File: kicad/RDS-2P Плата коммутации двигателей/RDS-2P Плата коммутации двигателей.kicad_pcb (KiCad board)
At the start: 2 copper layers, 100 x 100 mm, 12 parts, among them J1 XT30U, J2 XT30U, J3 5264-3AW, J4 5264-3AW, J5 5264-3AW, J6 5264-3AW, J7 Conn_01x01_Pin, J8 Conn_01x01_Pin, J9 Conn_01x01_Pin, U1 Converter_Mini560

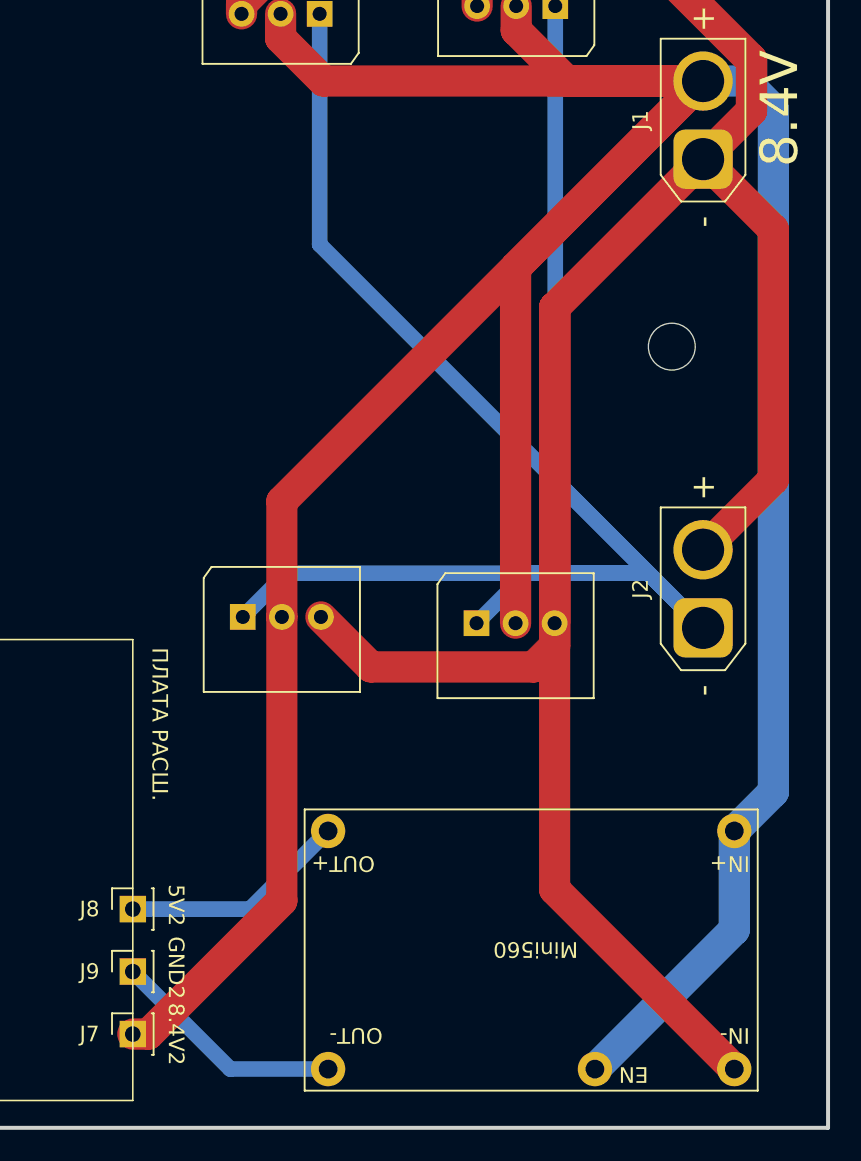
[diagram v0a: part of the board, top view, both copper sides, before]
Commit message: Fix: pinout Mini560
Исправил распиновку Mini560 на платах
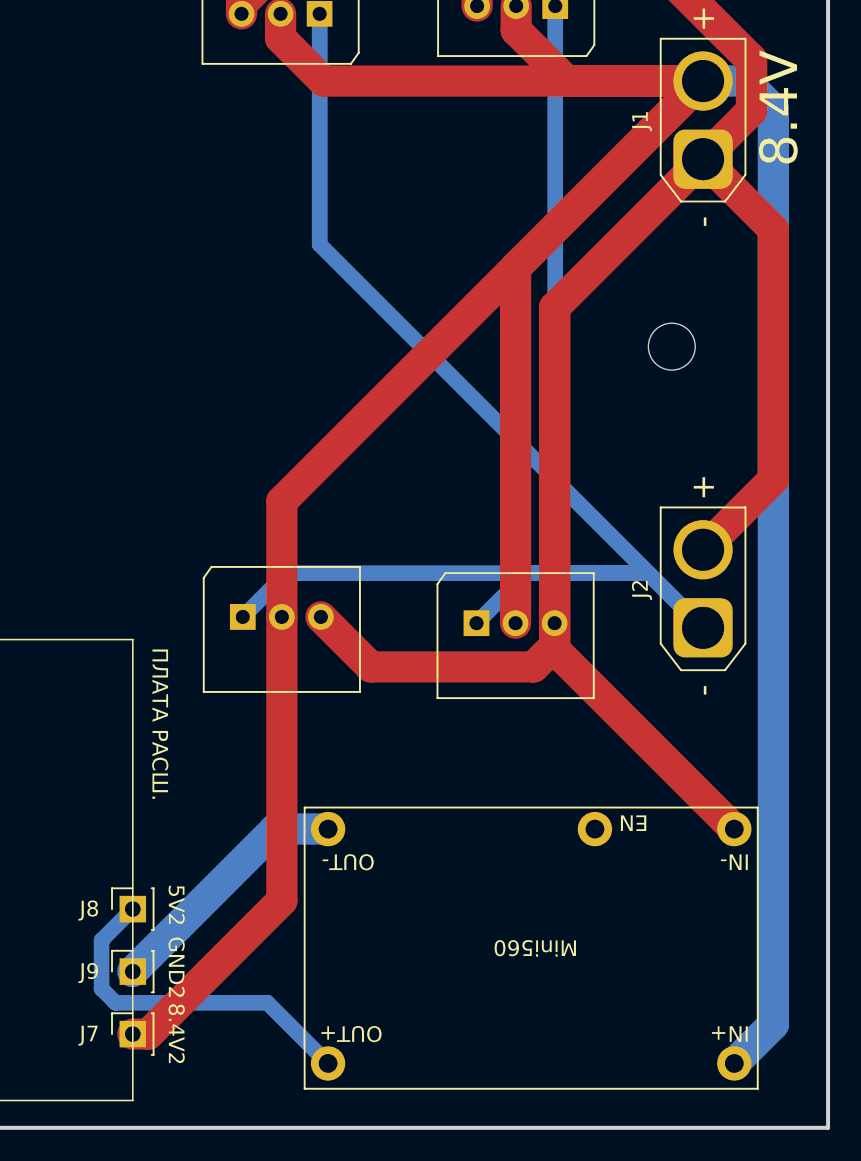
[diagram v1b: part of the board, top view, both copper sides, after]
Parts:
- moved U1 0.12 mm to (180.0, 131.9)
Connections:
- U1 pad 5: +8.4V -> 0 1
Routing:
- net 0: track 224.9 -> 189.3 mm
- net Net-(J8-Pin_1): track 14.6 -> 22.4 mm
- net +8.4V: track 232.4 -> 228.3 mm
- net Net-(J9-Pin_1): track 15.1 -> 16.3 mm
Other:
- board text removed: "EN"
- board text removed: "IN+"
- board text removed: "IN-"
- board text removed: "Mini560"
- board text removed: "OUT+"
- board text removed: "OUT-"
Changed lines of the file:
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@@
 	(net 4 "Net-(J8-Pin_1)")
 	(net 5 "Net-(J9-Pin_1)")
+	(net 6 "0 1")
 	(footprint "Connector_PinSocket_2.54mm:PinSocket_1x01_P2.54mm_Vertical"
 		(layer "F.Cu")
@@
 		(property ki_fp_filters "Connector*:*_1x??_*")
 		(sheetname "/")
-		(sheetfile "Плата коммутации двигателей для RDS-2P.kicad_sch")
+		(sheetfile "RDS-2P Плата коммутации двигателей.kicad_sch")
 		(attr through_hole)
 		(fp_line
@@
 		)
 		(sheetname "/")
-		(sheetfile "Плата коммутации двигателей для RDS-2P.kicad_sch")
+		(sheetfile "RDS-2P Плата коммутации двигателей.kicad_sch")
 		(fp_line
 			(start -2.5 4.8)
@@
 		(property ki_fp_filters "Connector*:*_1x??_*")
 		(sheetname "/")
-		(sheetfile "Плата коммутации двигателей для RDS-2P.kicad_sch")
+		(sheetfile "RDS-2P Плата коммутации двигателей.kicad_sch")
 		(attr through_hole)
 		(fp_line
@@
 		)
 		(sheetname "/")
-		(sheetfile "Плата коммутации двигателей для RDS-2P.kicad_sch")
+		(sheetfile "RDS-2P Плата коммутации двигателей.kicad_sch")
 		(fp_line
 			(start 7.5 4.8)
@@
 		)
 		(sheetname "/")
-		(sheetfile "Плата коммутации двигателей для RDS-2P.kicad_sch")
+		(sheetfile "RDS-2P Плата коммутации двигателей.kicad_sch")
 		(attr through_hole)
 		(fp_line
@@
 		)
 		(sheetname "/")
-		(sheetfile "Плата коммутации двигателей для RDS-2P.kicad_sch")
+		(sheetfile "RDS-2P Плата коммутации двигателей.kicad_sch")
 		(fp_line
 			(start -2.5 4.8)
@@
 		(property ki_fp_filters "Connector*:*_1x??_*")
 		(sheetname "/")
-		(sheetfile "Плата коммутации двигателей для RDS-2P.kicad_sch")
+		(sheetfile "RDS-2P Плата коммутации двигателей.kicad_sch")
 		(attr through_hole)
 		(fp_line
@@
 	(footprint "Library:Regulator_Mini560_5V"
 		(layer "F.Cu")
-		(at 180 132 180)
+		(at 180 131.88 180)
 		(property "Reference" "U1"
 			(at 13 -18.5 0)
@@
 		)
 		(sheetname "/")
-		(sheetfile "Плата коммутации двигателей для RDS-2P.kicad_sch")
+		(sheetfile "RDS-2P Плата коммутации двигателей.kicad_sch")
 		(fp_line
 			(start 27.5 1.38)
@@
 			(layer "F.CrtYd")
 		)
+		(fp_text user "Mini560"
+			(at 10 -7 180)
+			(unlocked yes)
+			(layer "F.SilkS")
+			(effects
+				(font
+					(size 1 1)
+					(thickness 0.1)
+				)
+				(justify left bottom)
+			)
+		)
+		(fp_text user "EN"
+			(at 5.5 1 180)
+			(unlocked yes)
+			(layer "F.SilkS")
+			(effects
+				(font
+					(size 1 1)
+					(thickness 0.1)
+				)
+				(justify left bottom)
+			)
+		)
+		(fp_text user "IN-"
+			(at -1 -1.5 180)
+			(unlocked yes)
+			(layer "F.SilkS")
+			(effects
+				(font
+					(size 1 1)
+					(thickness 0.1)
+				)
+				(justify left bottom)
+			)
+		)
+		(fp_text user "OUT-"
+			(at 23 -1.5 180)
+			(unlocked yes)
+			(layer "F.SilkS")
+			(effects
+				(font
+					(size 1 1)
+					(thickness 0.1)
+				)
+				(justify left bottom)
+			)
+		)
+		(fp_text user "OUT+"
+			(at 22.5 -12.5 180)
+			(unlocked yes)
+			(layer "F.SilkS")
+			(effects
+				(font
+					(size 1 1)
+					(thickness 0.1)
+				)
+				(justify left bottom)
+			)
+		)
+		(fp_text user "IN+"
+			(at -1 -12.5 180)
+			(unlocked yes)
+			(layer "F.SilkS")
+			(effects
+				(font
+					(size 1 1)
+					(thickness 0.1)
+				)
+				(justify left bottom)
+			)
+		)
 		(pad "1" thru_hole circle
-			(at 0 0 180)
+			(at 0 -15 180)
 			(size 2.2 2.2)
 			(drill 1.2)
@@
 		)
 		(pad "2" thru_hole circle
-			(at 0 -15.24 180)
+			(at 0 0 180)
 			(size 2.2 2.2)
 			(drill 1.2)
@@
 		)
 		(pad "3" thru_hole circle
-			(at 26 0 180)
+			(at 26 -15 180)
 			(size 2.2 2.2)
 			(drill 1.2)
@@
 		)
 		(pad "4" thru_hole circle
-			(at 26 -15.24 180)
+			(at 26 0 180)
 			(size 2.2 2.2)
 			(drill 1.2)
@@
 		)
 		(pad "5" thru_hole circle
-			(at 8.92 -15.24 180)
+			(at 8.92 0 180)
 			(size 2.2 2.2)
 			(drill 1.2)
 			(layers "*.Cu" "*.Mask")
 			(remove_unused_layers no)
-			(net 1 "+8.4V")
+			(net 6 "0 1")
 			(pinfunction "EN")
 			(pintype "input")
@@
 		)
 		(sheetname "/")
-		(sheetfile "Плата коммутации двигателей для RDS-2P.kicad_sch")
+		(sheetfile "RDS-2P Плата коммутации двигателей.kicad_sch")
 		(attr through_hole)
 		(fp_line
@@
 		)
 		(sheetname "/")
-		(sheetfile "Плата коммутации двигателей для RDS-2P.kicad_sch")
+		(sheetfile "RDS-2P Плата коммутации двигателей.kicad_sch")
 		(fp_line
 			(start 7.5 4.8)
@@
 		)
 	)
-	(gr_text "OUT-"
-		(at 157.5 144.5 180)
-		(layer "F.SilkS")
-		(effects
-			(font
-				(size 1 1)
-				(thickness 0.1)
-			)
-			(justify left bottom)
-		)
-	)
-	(gr_text "OUT+"
-		(at 157 133.5 180)
-		(layer "F.SilkS")
-		(effects
-			(font
-				(size 1 1)
-				(thickness 0.1)
-			)
-			(justify left bottom)
-		)
-	)
-	(gr_text "EN"
-		(at 174.5 147 180)
-		(layer "F.SilkS")
-		(effects
-			(font
-				(size 1 1)
-				(thickness 0.1)
-			)
-			(justify left bottom)
-		)
-	)
 	(gr_text "ПЛАТА РАСШ."
 		(at 142.635477 120.25 270)
@@
 		)
 	)
-	(gr_text "IN-"
-		(at 181 144.5 180)
-		(layer "F.SilkS")
-		(effects
-			(font
-				(size 1 1)
-				(thickness 0.1)
-			)
-			(justify left bottom)
-		)
-	)
 	(gr_text "8.4V"
 		(at 181.5 89.5 90)
@@
 		)
 	)
-	(gr_text "IN+"
-		(at 181 133.5 180)
-		(layer "F.SilkS")
-		(effects
-			(font
-				(size 1 1)
-				(thickness 0.1)
-			)
-			(justify left bottom)
-		)
-	)
-	(gr_text "Mini560"
-		(at 170 139 180)
-		(layer "F.SilkS")
-		(effects
-			(font
-				(size 1 1)
-				(thickness 0.1)
-			)
-			(justify left bottom)
-		)
-	)
 	(gr_text "RTU MIREA"
 		(at 147.5 54.5 0)
@@
 	)
 	(segment
-		(start 180 132)
-		(end 180 138.32)
+		(start 182.5 144.38)
+		(end 180 146.88)
 		(width 2)
 		(layer "B.Cu")
@@
 	)
 	(segment
-		(start 182.5 129.5)
-		(end 180 132)
-		(width 2)
-		(layer "B.Cu")
-		(net 1)
-	)
-	(segment
-		(start 180 138.32)
-		(end 171.08 147.24)
+		(start 182.5 85.812995)
+		(end 182.5 144.38)
 		(width 2)
 		(layer "B.Cu")
@@
 	)
 	(segment
-		(start 182.5 85.812995)
-		(end 182.5 129.5)
-		(width 2)
-		(layer "B.Cu")
-		(net 1)
-	)
-	(segment
 		(start 180.687005 84)
 		(end 182.5 85.812995)
@@
 	)
 	(segment
-		(start 168.5 98.5)
-		(end 168.5 135.74)
+		(start 181.101 82.715523)
+		(end 174.385477 76)
 		(width 2)
 		(layer "F.Cu")
@@
 	)
 	(segment
-		(start 168.5 135.74)
-		(end 180 147.24)
+		(start 182.5 93.5)
+		(end 182.5 109.5)
 		(width 2)
 		(layer "F.Cu")
@@
 	)
 	(segment
-		(start 181.101 82.715523)
-		(end 174.385477 76)
+		(start 168.5 118.7)
+		(end 168.5 120.38)
 		(width 2)
 		(layer "F.Cu")
@@
 	)
 	(segment
-		(start 182.5 93.5)
-		(end 182.5 109.5)
+		(start 165.573574 76)
+		(end 163.54 78.033574)
 		(width 2)
 		(layer "F.Cu")
@@
 	)
 	(segment
-		(start 165.573574 76)
-		(end 163.54 78.033574)
+		(start 181.101 85.899)
+		(end 181.101 82.601)
 		(width 2)
 		(layer "F.Cu")
@@
 	)
 	(segment
-		(start 181.101 85.899)
-		(end 181.101 82.601)
+		(start 168.5 120.38)
+		(end 180 131.88)
 		(width 2)
 		(layer "F.Cu")
@@
 	)
 	(segment
-		(start 154 132)
-		(end 149 137)
+		(start 139.5 139)
+		(end 141.5 137)
 		(width 1)
 		(layer "B.Cu")
@@
 	)
 	(segment
-		(start 149 137)
-		(end 141.5 137)
+		(start 150.12 143)
+		(end 140.398 143)
+		(width 1)
+		(layer "B.Cu")
+		(net 4)
+	)
+	(segment
+		(start 139.5 142.102)
+		(end 139.5 139)
 		(width 1)
 		(layer "B.Cu")
@@
 	)
 	(segment
-		(start 154 147.24)
-		(end 147.74 147.24)
+		(start 140.398 143)
+		(end 139.5 142.102)
 		(width 1)
 		(layer "B.Cu")
+		(net 4)
+	)
+	(segment
+		(start 154 146.88)
+		(end 150.12 143)
+		(width 1)
+		(layer "B.Cu")
+		(net 4)
+	)
+	(segment
+		(start 154 131.88)
+		(end 150.62 131.88)
+		(width 2)
+		(layer "B.Cu")
 		(net 5)
 	)
 	(segment
-		(start 147.74 147.24)
+		(start 150.62 131.88)
 		(end 141.5 141)
-		(width 1)
+		(width 2)
 		(layer "B.Cu")
 		(net 5)
